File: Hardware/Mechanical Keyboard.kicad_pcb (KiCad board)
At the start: 2 copper layers, 343.4 x 105.3 mm, 260 parts, among them J1 USBMINI_B05, U1 ATMEGA32U4-AU, U2 IS31FL3731-SALS2, X1 ASX4

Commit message: Keyboard tracking was finished. Only GND circuit is left
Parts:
- moved C6 65.4 mm to (332.0, 96.5), turned to 270 degrees
- moved R8 59.1 mm to (342.3, 138.3), turned to 90 degrees
- moved R10 58.2 mm to (338.5, 133.0)
- moved C5 48.1 mm to (348.9, 144.7), turned to 0 degrees
- moved S101 48.0 mm to (351.8, 133.1)
- moved X1 45.1 mm to (351.9, 133.1)
- moved C2 43.9 mm to (345.5, 133.2), turned to 0 degrees
- moved R13 42.5 mm to (348.4, 154.3)
- moved C3 41.1 mm to (358.0, 133.1), turned to 180 degrees
- moved R11 40.8 mm to (348.9, 148.5), turned to 180 degrees
- moved R1 39.9 mm to (351.9, 128.5)
- moved R12 38.7 mm to (348.5, 152.1)
- moved R9 32.9 mm to (357.8, 146.9), turned to 270 degrees
- moved R100 30.8 mm to (376.2, 180.9), turned to 270 degrees
- moved R4 24.2 mm to (376.3, 149.9), turned to 180 degrees
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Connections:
- J1 pad 4: (no net) -> Net-(J1-Pad4)
- LED19 pad 2: (no net) -> Net-(LED19-Pad2)
- S101 pad 2: (no net) -> Net-(S101-Pad2)
- S101 pad 4: (no net) -> Net-(S101-Pad4)
- U1 pad 10: /swm_row3 -> /swm_col6
- U1 pad 11: /swm_row4 -> /swm_col8
- U1 pad 12: /swm_row5 -> /swm_col10
- U1 pad 21: /swm_col1 -> /swm_col12
- U1 pad 22: /swm_col3 -> /swm_col14
- U1 pad 25: /swm_col5 -> /swm_row1
- U1 pad 26: /swm_col7 -> /swm_row2
- U1 pad 27: /swm_col14 -> /swm_row3
- U1 pad 28: /swm_col12 -> /swm_row4
- U1 pad 29: /swm_col10 -> /swm_row5
- U1 pad 30: /swm_col8 -> /swm_col13
- U1 pad 31: /swm_col6 -> /swm_co11
- U1 pad 36: /swm_col4 -> /swm_col7
- U1 pad 37: /swm_col11 -> /swm_col5
- U1 pad 38: /swm_col13 -> /swm_col3
- U1 pad 40: /swm_col2 -> /swm_col1
- U1 pad 8: /swm_row1 -> /swm_col2
- U1 pad 9: /swm_row2 -> /swm_col4
- U2 pad 10: (no net) -> Net-(U2-Pad10)
- U2 pad 11: (no net) -> Net-(U2-Pad11)
- U2 pad 12: (no net) -> Net-(U2-Pad12)
- U2 pad 13: (no net) -> Net-(U2-Pad13)
- U2 pad 14: (no net) -> Net-(U2-Pad14)
- U2 pad 15: (no net) -> Net-(U2-Pad15)
- U2 pad 17: (no net) -> Net-(U2-Pad17)
- U2 pad 7: (no net) -> Net-(U2-Pad7)
- U2 pad 8: (no net) -> Net-(U2-Pad8)
- U2 pad 9: (no net) -> Net-(U2-Pad9)
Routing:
- net VCC: track 7.21 -> 981.8 mm, vias 1 -> 17
- net Net-(LED105-Pad2): track 0.00 -> 106.5 mm
- net /led_ca8: track 429.3 -> 525.5 mm, vias 10 -> 14
- net /led_ca3: track 457.2 -> 541.6 mm, vias 3 -> 5
- net /led_ca2: track 496.3 -> 577.5 mm, vias 5 -> 7
- net Net-(LED102-Pad2): track 0.00 -> 79.3 mm
- net Net-(LED108-Pad2): track 0.00 -> 78.1 mm
- net Net-(LED107-Pad2): track 0.00 -> 77.1 mm
- net Net-(LED104-Pad2): track 0.00 -> 75.9 mm
- net Net-(LED103-Pad2): track 0.00 -> 74.3 mm
- net Net-(LED101-Pad2): track 0.00 -> 73.4 mm
- net Net-(LED106-Pad2): track 0.00 -> 72.6 mm
- net Net-(LED109-Pad2): track 0.00 -> 72.2 mm
- net /rgb_bl: track 0.00 -> 67.4 mm, vias 0 -> 3
- net Net-(R3-Pad1): track 0.00 -> 66.5 mm, vias 0 -> 3
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
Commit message: Small refactoring
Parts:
- moved C5 0.38 mm to (348.5, 144.7)
- moved R11 0.30 mm to (348.6, 148.5)
- moved R10 0.28 mm to (338.5, 133.3)
- moved R13 0.10 mm to (348.5, 154.3)
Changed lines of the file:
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@@
   )
   (module Capacitors_SMD:C_0805_HandSoldering (layer F.Cu)
-    (at 348.889 144.653)
+    (at 348.508 144.7038)
     (descr "Capacitor SMD 0805, hand soldering")
     (tags "capacitor 0805")
@@
   )
   (module Resistors_SMD:R_0805_HandSoldering (layer F.Cu)
-    (at 338.5058 132.9944 180)
+    (at 338.502 133.2738 180)
     (descr "Resistor SMD 0805, hand soldering")
     (tags "resistor 0805")
@@
   )
   (module Resistors_SMD:R_0805_HandSoldering (layer B.Cu)
-    (at 348.869 148.463 180)
+    (at 348.568 148.4884 180)
     (descr "Resistor SMD 0805, hand soldering")
     (tags "resistor 0805")
@@
   )
   (module Resistors_SMD:R_0805_HandSoldering (layer F.Cu)
-    (at 348.441 154.305 180)
+    (at 348.535 154.3304 180)
     (descr "Resistor SMD 0805, hand soldering")
     (tags "resistor 0805")
@@
   (segment (start 326.26 120.72) (end 326.26 122.05) (width 0.6) (layer F.Cu) (net 97))
   (via (at 326.26 122.05) (size 0.4) (drill 0.3) (layers F.Cu B.Cu) (net 97))
-  (segment (start 331.2 156.3) (end 331.724 156.3) (width 0.3) (layer F.Cu) (net 97))
   (segment (start 332.44 156.3) (end 335.09 156.3) (width 0.3) (layer F.Cu) (net 97))
   (segment (start 294.905457 80.146024) (end 360.054024 80.146024) (width 0.6) (layer F.Cu) (net 98))
@@
   (segment (start 331.724 127.514) (end 331.724 156.3) (width 0.3) (layer B.Cu) (net 97))
   (segment (start 326.26 122.05) (end 331.724 127.514) (width 0.3) (layer B.Cu) (net 97))
+  (segment (start 331.2 156.3) (end 331.724 156.3) (width 0.6) (layer F.Cu) (net 97))
   (segment (start 344.50001 103.35) (end 357.858 103.35) (width 0.6) (layer B.Cu) (net 110))
   (segment (start 357.858 103.35) (end 361.795 103.35) (width 0.6) (layer B.Cu) (net 110))

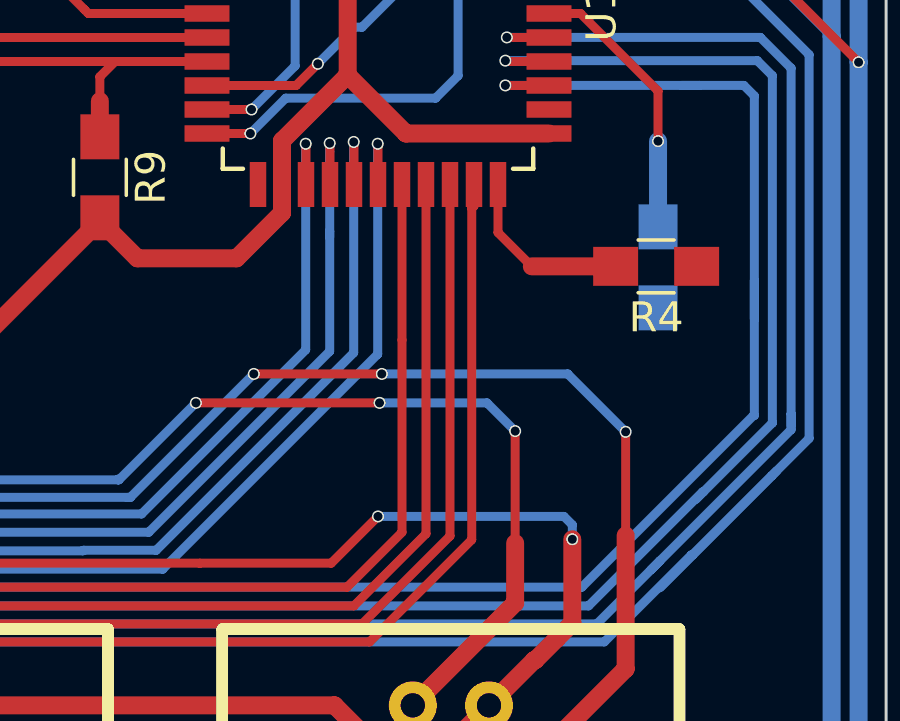
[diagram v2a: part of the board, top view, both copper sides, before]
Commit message: Bugfix for swm_col11 connection to atmega
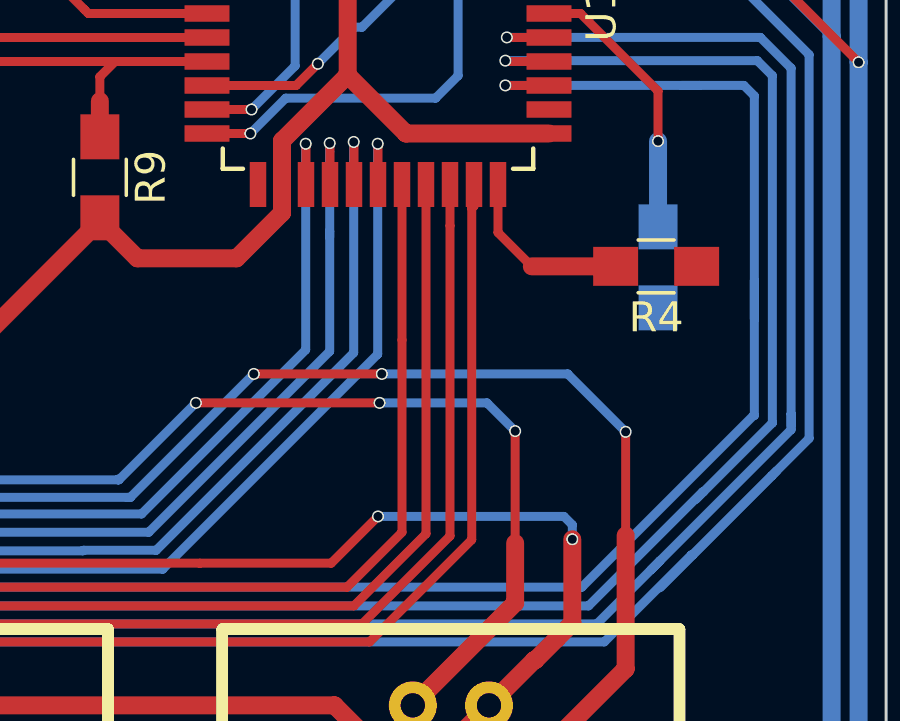
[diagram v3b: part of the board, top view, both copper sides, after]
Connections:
- U1 pad 31: /swm_co11 -> /swm_col11
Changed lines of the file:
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@@
     (thickness 1.6)
     (drawings 1632)
-    (tracks 3158)
+    (tracks 3159)
     (zones 0)
     (modules 260)
-    (nets 147)
+    (nets 146)
   )
   (page A3)
@@
   (net 144 "Net-(U2-Pad15)")
   (net 145 "Net-(U2-Pad17)")
-  (net 146 /swm_co11)
   (net_class Default "Это класс цепей по умолчанию."
     (clearance 0.1)
@@
     (add_net /rgb-backlight/data_input)
     (add_net /rgb_bl)
-    (add_net /swm_co11)
     (add_net /swm_col1)
     (add_net /swm_col10)
@@
       (net 68 /swm_col13))
     (pad 31 smd rect (at 5.7 -2.4 270) (size 1.5 0.55) (layers F.Cu F.Paste F.Mask)
-      (net 146 /swm_co11))
+      (net 56 /swm_col11))
     (pad 32 smd rect (at 5.7 -3.2 270) (size 1.5 0.55) (layers F.Cu F.Paste F.Mask)
       (net 46 /swm_col9))
@@
   (segment (start 330.214889 173.910111) (end 330.214889 173.910111) (width 0.6) (layer B.Cu) (net 56))
   (via (at 330.214889 173.910111) (size 0.6) (drill 0.4) (layers F.Cu B.Cu) (net 56))
-  (segment (start 369.43 147.178) (end 369.43 158.895) (width 0.3) (layer F.Cu) (net 56))
   (segment (start 369.43 158.895) (end 366.5 161.825) (width 0.3) (layer F.Cu) (net 56))
   (segment (start 366.5 161.825) (end 344.625 161.825) (width 0.3) (layer F.Cu) (net 56))
@@
   (segment (start 330.214889 171.385111) (end 330.214889 173.910111) (width 0.3) (layer F.Cu) (net 56))
   (segment (start 332.1 169.5) (end 330.214889 171.385111) (width 0.3) (layer F.Cu) (net 56))
+  (segment (start 369.43 158.895) (end 369.43 148.5522) (width 0.3) (layer F.Cu) (net 56))
+  (segment (start 369.43 148.5522) (end 369.43 147.178) (width 0.3) (layer F.Cu) (net 56))
   (segment (start 242.858 101.854) (end 241.808 101.854) (width 0.6) (layer B.Cu) (net 57))
   (segment (start 243.08 98.54) (end 243.08 101.632) (width 0.6) (layer B.Cu) (net 57))

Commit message: Temporary solution with GND filling
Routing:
- net GND: track 0.27 -> 13.2 mm, vias 0 -> 14
- net VCC: track 981.8 -> 982.9 mm, vias 17 -> 19
- net /swm_col14: track 263.3 -> 262.7 mm
- net /led_ca8: track 525.5 -> 525.9 mm, vias 14 -> 16
- net /swm_col15: track 150.6 -> 150.8 mm, vias 1 -> 3
- net /swm_col6: vias 4 -> 3
- added copper zone on B.Cu, net GND
- added copper zone on F.Cu, net GND
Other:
- net class Default: via_dia 0.4 -> 0.7; via_drill 0.3 -> 0.4

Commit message: GND curcuit fill was finished
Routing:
- net GND: vias 14 -> 57
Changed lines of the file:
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@@
     (thickness 1.6)
     (drawings 1632)
-    (tracks 3205)
+    (tracks 3248)
     (zones 0)
     (modules 260)
@@
   (via (at 44.196 181.356) (size 0.7) (drill 0.4) (layers F.Cu B.Cu) (net 88))
   (via (at 164.3888 151.638) (size 0.7) (drill 0.4) (layers F.Cu B.Cu) (net 88))
+  (via (at 356.5906 108.0262) (size 0.7) (drill 0.4) (layers F.Cu B.Cu) (net 88))
+  (via (at 168.1226 120.269) (size 0.7) (drill 0.4) (layers F.Cu B.Cu) (net 88))
+  (via (at 191.2366 140.7668) (size 0.7) (drill 0.4) (layers F.Cu B.Cu) (net 88))
+  (via (at 283.5402 119.5578) (size 0.7) (drill 0.4) (layers F.Cu B.Cu) (net 88))
+  (via (at 312.7502 108.2548) (size 0.7) (drill 0.4) (layers F.Cu B.Cu) (net 88))
+  (via (at 322.1736 130.5052) (size 0.7) (drill 0.4) (layers F.Cu B.Cu) (net 88))
+  (via (at 332.0796 122.5804) (size 0.7) (drill 0.4) (layers F.Cu B.Cu) (net 88))
+  (via (at 338.836 127.2032) (size 0.7) (drill 0.4) (layers F.Cu B.Cu) (net 88))
+  (via (at 173.5836 168.2242) (size 0.7) (drill 0.4) (layers F.Cu B.Cu) (net 88))
+  (via (at 173.4312 161.4932) (size 0.7) (drill 0.4) (layers F.Cu B.Cu) (net 88))
+  (via (at 114.0714 162.306) (size 0.7) (drill 0.4) (layers F.Cu B.Cu) (net 88))
+  (via (at 217.4748 162.6616) (size 0.7) (drill 0.4) (layers F.Cu B.Cu) (net 88))
+  (via (at 260.1468 158.4198) (size 0.7) (drill 0.4) (layers F.Cu B.Cu) (net 88))
+  (via (at 93.218 109.0168) (size 0.7) (drill 0.4) (layers F.Cu B.Cu) (net 88))
+  (via (at 131.7752 111.4552) (size 0.7) (drill 0.4) (layers F.Cu B.Cu) (net 88))
+  (via (at 294.4114 101.346) (size 0.7) (drill 0.4) (layers F.Cu B.Cu) (net 88))
+  (via (at 287.9344 145.4912) (size 0.7) (drill 0.4) (layers F.Cu B.Cu) (net 88))
+  (via (at 290.068 151.13) (size 0.7) (drill 0.4) (layers F.Cu B.Cu) (net 88))
+  (via (at 356.9716 152.7556) (size 0.7) (drill 0.4) (layers F.Cu B.Cu) (net 88))
+  (via (at 334.7212 161.5948) (size 0.7) (drill 0.4) (layers F.Cu B.Cu) (net 88))
+  (via (at 102.3366 92.7608) (size 0.7) (drill 0.4) (layers F.Cu B.Cu) (net 88))
+  (via (at 84.074 88.2904) (size 0.7) (drill 0.4) (layers F.Cu B.Cu) (net 88))
+  (via (at 100.965 88.519) (size 0.7) (drill 0.4) (layers F.Cu B.Cu) (net 88))
+  (via (at 121.9962 88.4682) (size 0.7) (drill 0.4) (layers F.Cu B.Cu) (net 88))
+  (via (at 311.6834 150.4696) (size 0.7) (drill 0.4) (layers F.Cu B.Cu) (net 88))
+  (via (at 291.6174 155.7274) (size 0.7) (drill 0.4) (layers F.Cu B.Cu) (net 88))
+  (via (at 248.7168 80.1116) (size 0.7) (drill 0.4) (layers F.Cu B.Cu) (net 88))
+  (via (at 264.16 148.5392) (size 0.7) (drill 0.4) (layers F.Cu B.Cu) (net 88))
+  (via (at 293.624 168.6306) (size 0.7) (drill 0.4) (layers F.Cu B.Cu) (net 88))
+  (via (at 311.3024 137.9982) (size 0.7) (drill 0.4) (layers F.Cu B.Cu) (net 88))
+  (via (at 287.8836 165.9382) (size 0.7) (drill 0.4) (layers F.Cu B.Cu) (net 88))
+  (via (at 274.3708 174.8028) (size 0.7) (drill 0.4) (layers F.Cu B.Cu) (net 88))
+  (via (at 182.7276 180.086) (size 0.7) (drill 0.4) (layers F.Cu B.Cu) (net 88))
+  (via (at 140.7414 92.837) (size 0.7) (drill 0.4) (layers F.Cu B.Cu) (net 88))
+  (via (at 159.2326 92.7608) (size 0.7) (drill 0.4) (layers F.Cu B.Cu) (net 88))
+  (via (at 179.3748 92.1512) (size 0.7) (drill 0.4) (layers F.Cu B.Cu) (net 88))
+  (via (at 216.3826 92.5322) (size 0.7) (drill 0.4) (layers F.Cu B.Cu) (net 88))
+  (via (at 198.2978 92.9132) (size 0.7) (drill 0.4) (layers F.Cu B.Cu) (net 88))
+  (via (at 255.143 92.3798) (size 0.7) (drill 0.4) (layers F.Cu B.Cu) (net 88))
+  (via (at 275.2344 93.3704) (size 0.7) (drill 0.4) (layers F.Cu B.Cu) (net 88))
+  (via (at 236.982 93.218) (size 0.7) (drill 0.4) (layers F.Cu B.Cu) (net 88))
+  (via (at 315.4172 91.44) (size 0.7) (drill 0.4) (layers F.Cu B.Cu) (net 88))
+  (via (at 359.9434 165.608) (size 0.7) (drill 0.4) (layers F.Cu B.Cu) (net 88))
   (segment (start 368.19 164.54) (end 371.602 161.128) (width 0.6) (layer F.Cu) (net 89))
   (segment (start 371.602 161.128) (end 371.602 159.131) (width 0.6) (layer F.Cu) (net 89))

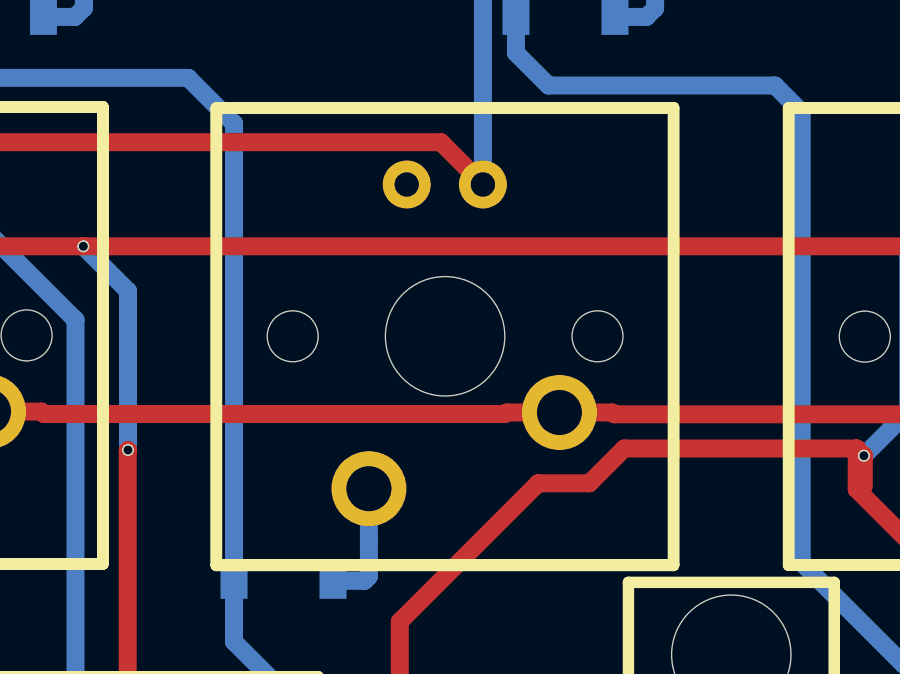
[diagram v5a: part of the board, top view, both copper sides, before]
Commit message: Bugfix for swm_col9
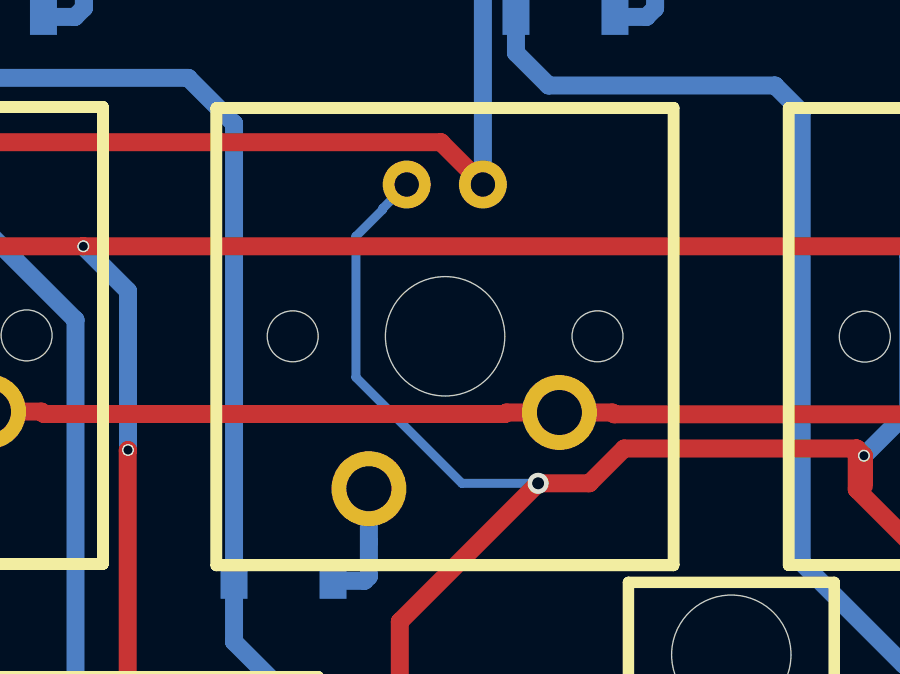
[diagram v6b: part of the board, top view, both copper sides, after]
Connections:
- LED19 pad 2: Net-(LED19-Pad2) -> /led_ca9
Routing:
- net /led_ca9: track 505.6 -> 520.3 mm, vias 14 -> 15
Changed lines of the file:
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@@
     (thickness 1.6)
     (drawings 1632)
-    (tracks 3248)
+    (tracks 3256)
     (zones 0)
     (modules 260)
-    (nets 146)
+    (nets 145)
   )
   (page A3)
@@
   (net 131 "Net-(R8-Pad1)")
   (net 132 "Net-(J1-Pad4)")
-  (net 133 "Net-(LED19-Pad2)")
-  (net 134 "Net-(S101-Pad4)")
-  (net 135 "Net-(S101-Pad2)")
-  (net 136 "Net-(U2-Pad7)")
-  (net 137 "Net-(U2-Pad8)")
-  (net 138 "Net-(U2-Pad9)")
-  (net 139 "Net-(U2-Pad10)")
-  (net 140 "Net-(U2-Pad11)")
-  (net 141 "Net-(U2-Pad12)")
-  (net 142 "Net-(U2-Pad13)")
-  (net 143 "Net-(U2-Pad14)")
-  (net 144 "Net-(U2-Pad15)")
-  (net 145 "Net-(U2-Pad17)")
+  (net 133 "Net-(S101-Pad4)")
+  (net 134 "Net-(S101-Pad2)")
+  (net 135 "Net-(U2-Pad7)")
+  (net 136 "Net-(U2-Pad8)")
+  (net 137 "Net-(U2-Pad9)")
+  (net 138 "Net-(U2-Pad10)")
+  (net 139 "Net-(U2-Pad11)")
+  (net 140 "Net-(U2-Pad12)")
+  (net 141 "Net-(U2-Pad13)")
+  (net 142 "Net-(U2-Pad14)")
+  (net 143 "Net-(U2-Pad15)")
+  (net 144 "Net-(U2-Pad17)")
   (net_class Default "Это класс цепей по умолчанию."
     (clearance 0.1)
@@
     (add_net "Net-(LED109-Pad2)")
     (add_net "Net-(LED110-Pad2)")
-    (add_net "Net-(LED19-Pad2)")
     (add_net "Net-(R1-Pad2)")
     (add_net "Net-(R11-Pad2)")
@@
       (net 88 GND))
     (pad 4 smd rect (at 4.45 -1.999) (size 3.1 1) (layers B.Cu B.Paste B.Mask)
-      (net 134 "Net-(S101-Pad4)"))
+      (net 133 "Net-(S101-Pad4)"))
     (pad 2 smd rect (at 4.45 1.999) (size 3.1 1) (layers B.Cu B.Paste B.Mask)
-      (net 135 "Net-(S101-Pad2)"))
+      (net 134 "Net-(S101-Pad2)"))
     (pad 3 smd rect (at -4.45 -1.999) (size 3.1 1) (layers B.Cu B.Paste B.Mask)
       (net 114 "Net-(R1-Pad2)"))
@@
       (net 129 "Net-(R11-Pad2)"))
     (pad 7 smd rect (at -1.95 1.2 90) (size 0.8 0.2) (layers F.Cu F.Paste F.Mask)
-      (net 136 "Net-(U2-Pad7)"))
+      (net 135 "Net-(U2-Pad7)"))
     (pad 8 smd rect (at -1.2 1.95 180) (size 0.8 0.2) (layers F.Cu F.Paste F.Mask)
-      (net 137 "Net-(U2-Pad8)"))
+      (net 136 "Net-(U2-Pad8)"))
     (pad 9 smd rect (at -0.8 1.95 180) (size 0.8 0.2) (layers F.Cu F.Paste F.Mask)
-      (net 138 "Net-(U2-Pad9)"))
+      (net 137 "Net-(U2-Pad9)"))
     (pad 10 smd rect (at -0.4 1.95 180) (size 0.8 0.2) (layers F.Cu F.Paste F.Mask)
-      (net 139 "Net-(U2-Pad10)"))
+      (net 138 "Net-(U2-Pad10)"))
     (pad 11 smd rect (at 0 1.95 180) (size 0.8 0.2) (layers F.Cu F.Paste F.Mask)
-      (net 140 "Net-(U2-Pad11)"))
+      (net 139 "Net-(U2-Pad11)"))
     (pad 12 smd rect (at 0.4 1.95 180) (size 0.8 0.2) (layers F.Cu F.Paste F.Mask)
-      (net 141 "Net-(U2-Pad12)"))
+      (net 140 "Net-(U2-Pad12)"))
     (pad 13 smd rect (at 0.8 1.95 180) (size 0.8 0.2) (layers F.Cu F.Paste F.Mask)
-      (net 142 "Net-(U2-Pad13)"))
+      (net 141 "Net-(U2-Pad13)"))
     (pad 14 smd rect (at 1.2 1.95 180) (size 0.8 0.2) (layers F.Cu F.Paste F.Mask)
-      (net 143 "Net-(U2-Pad14)"))
+      (net 142 "Net-(U2-Pad14)"))
     (pad 15 smd rect (at 1.95 1.2 90) (size 0.8 0.2) (layers F.Cu F.Paste F.Mask)
-      (net 144 "Net-(U2-Pad15)"))
+      (net 143 "Net-(U2-Pad15)"))
     (pad 16 smd rect (at 1.95 0.8 90) (size 0.8 0.2) (layers F.Cu F.Paste F.Mask)
       (net 130 "Net-(C5-Pad1)"))
     (pad 17 smd rect (at 1.95 0.4 90) (size 0.8 0.2) (layers F.Cu F.Paste F.Mask)
-      (net 145 "Net-(U2-Pad17)"))
+      (net 144 "Net-(U2-Pad17)"))
     (pad 18 smd rect (at 1.95 0 90) (size 0.8 0.2) (layers F.Cu F.Paste F.Mask)
       (net 131 "Net-(R8-Pad1)"))
@@
       (net 97 /led_ca7))
     (pad 2 thru_hole circle (at 1.27 5.08 180) (size 1.6002 1.6002) (drill 0.8128) (layers *.Cu *.Mask)
-      (net 133 "Net-(LED19-Pad2)"))
+      (net 89 /led_ca9))
     (model LEDs.3dshapes/LED-3MM.wrl
       (offset (xyz 0 -5.079999923706055 6.349999904632568))
@@
   (segment (start 370.6622 154.4574) (end 371.602 155.3972) (width 0.3) (layer B.Cu) (net 89))
   (segment (start 367.0808 154.4574) (end 370.6622 154.4574) (width 0.3) (layer B.Cu) (net 89))
+  (segment (start 139.17 155.5) (end 139.17 155.5) (width 0.6) (layer F.Cu) (net 89))
+  (via (at 139.17 155.5) (size 0.7) (drill 0.4) (layers F.Cu B.Cu) (net 89))
+  (segment (start 133.989901 146.340099) (end 133.989901 146.375299) (width 0.3) (layer B.Cu) (net 89))
+  (segment (start 134.79 145.54) (end 133.989901 146.340099) (width 0.3) (layer B.Cu) (net 89))
+  (segment (start 133.989901 146.375299) (end 133.096 147.2692) (width 0.3) (layer B.Cu) (net 89))
+  (segment (start 133.096 147.2692) (end 133.096 151.9682) (width 0.3) (layer B.Cu) (net 89))
+  (segment (start 136.6278 155.5) (end 139.17 155.5) (width 0.3) (layer B.Cu) (net 89))
+  (segment (start 133.096 151.9682) (end 136.6278 155.5) (width 0.3) (layer B.Cu) (net 89))
   (segment (start 368.18 107.41) (end 366.522 109.068) (width 0.6) (layer F.Cu) (net 91))
   (segment (start 366.522 109.068) (end 366.522 113.538) (width 0.6) (layer F.Cu) (net 91))

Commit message: add driling holes
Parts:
- added REF**: MountingHole_3.2mm_M3, MountingHole:MountingHole_3.2mm_M3, F.Cu at (380.0, 82.8)
- added REF**: MountingHole_3.2mm_M3, MountingHole:MountingHole_3.2mm_M3, F.Cu at (380.2, 180.5)
- added REF**: MountingHole_3.2mm_M3, MountingHole:MountingHole_3.2mm_M3, F.Cu at (44.3, 180.4)
- added REF**: MountingHole_3.2mm_M3, MountingHole:MountingHole_3.2mm_M3, F.Cu at (44.1, 82.7)
- added REF**: MountingHole_3.2mm_M3, MountingHole:MountingHole_3.2mm_M3, F.Cu at (150.8, 140.8)
- added REF**: MountingHole_3.2mm_M3, MountingHole:MountingHole_3.2mm_M3, F.Cu at (246.6, 139.0)
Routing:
- net VCC: track 982.9 -> 980.5 mm
- net Net-(LED105-Pad2): track 106.5 -> 105.3 mm
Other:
- net class Default: trace_width 0.3 -> 0.6
